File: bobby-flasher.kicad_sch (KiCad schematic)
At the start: 20 parts, among them J1 Conn_01x03, J2 Conn_01x06, J3 Flash, Q1 SS8050_C2150, Q2 SS8050_C2150, U1 CH343G, U2 AMS1117-3.3

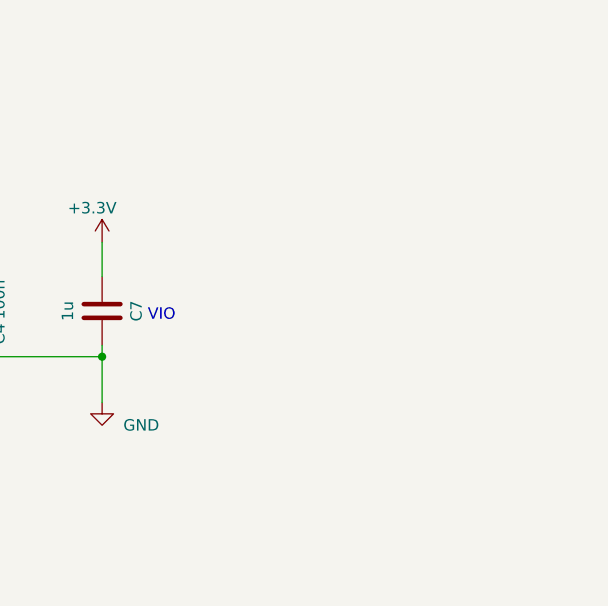
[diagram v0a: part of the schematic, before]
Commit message: new layout, added leds
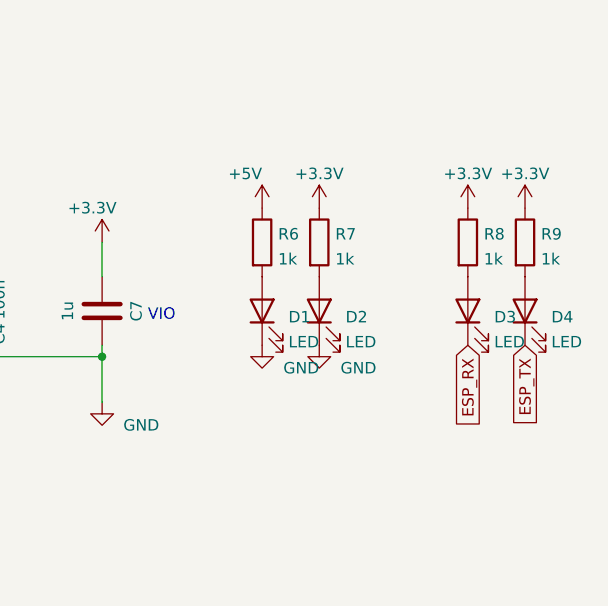
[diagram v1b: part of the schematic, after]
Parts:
- added D1, D2, D3, D4: LED, LED_SMD:LED_0603_1608Metric, symbol Device:LED
- added R6, R7, R8, R9: 1k, Resistor_SMD:R_0402_1005Metric, symbol Device:R
- C1, C3, C4, C6: footprint Capacitor_SMD:C_0603_1608Metric -> Capacitor_SMD:C_0402_1005Metric
- R1, R2, R3, R4, R5: footprint Resistor_SMD:R_0603_1608Metric -> Resistor_SMD:R_0402_1005Metric
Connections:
- net +3V3: now also R7.1, R8.1, R9.1
- net +5V: now also R6.1
- net ESP_RX: now also D3.1 (K)
- net ESP_TX: now also D4.1 (K)
- net GND: now also D1.1 (K), D2.1 (K)
- new net: D1.2 (A), R6.2
- new net: D3.2 (A), R8.2
- new net: D2.2 (A), R7.2
- new net: D4.2 (A), R9.2

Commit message: Updated files
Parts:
- C1, C3, C4, C6: LCSC Part # C14663 -> C1525
- D1: LCSC (none) -> C2286
- D2: LCSC (none) -> C72043
- D3: LCSC (none) -> C2290
- D4: LCSC (none) -> C72041
- J3: LCSC (none) -> C5663
- R1, R3: LCSC C23186 -> C25905
- R2: LCSC C25804 -> C25744
- R4, R5: LCSC C22790 -> C25752
- R6, R7, R8, R9: LCSC (none) -> C11702
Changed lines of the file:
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@@
       (effects (font (size 1.27 1.27)) hide)
     )
-    (property "LCSC Part #" "C14663" (id 4) (at 132.08 125.73 90)
+    (property "LCSC Part #" "C1525" (id 4) (at 132.08 125.73 90)
       (effects (font (size 1.27 1.27)) hide)
     )
@@
       (effects (font (size 1.27 1.27)) hide)
     )
-    (property "LCSC" "C22790" (id 4) (at 162.56 151.13 90)
+    (property "LCSC" "C25752" (id 4) (at 162.56 151.13 90)
       (effects (font (size 1.27 1.27)) hide)
     )
@@
     )
     (property "Datasheet" "~" (id 3) (at 166.37 88.9 0)
+      (effects (font (size 1.27 1.27)) hide)
+    )
+    (property "LCSC" "C11702" (id 4) (at 166.37 88.9 0)
       (effects (font (size 1.27 1.27)) hide)
     )
@@
       (effects (font (size 1.27 1.27)) hide)
     )
-    (property "LCSC Part #" "C14663" (id 4) (at 93.98 180.34 90)
+    (property "LCSC Part #" "C1525" (id 4) (at 93.98 180.34 90)
       (effects (font (size 1.27 1.27)) hide)
     )
@@
     )
     (property "Datasheet" "~" (id 3) (at 189.23 96.52 0)
+      (effects (font (size 1.27 1.27)) hide)
+    )
+    (property "LCSC" "C2290" (id 4) (at 189.23 96.52 90)
       (effects (font (size 1.27 1.27)) hide)
     )
@@
       (effects (font (size 1.27 1.27)) hide)
     )
+    (property "LCSC" "C2286" (id 4) (at 166.37 96.52 90)
+      (effects (font (size 1.27 1.27)) hide)
+    )
     (pin "1")
     (pin "2")
@@
       (effects (font (size 1.27 1.27)) hide)
     )
+    (property "LCSC" "C72043" (id 4) (at 172.72 96.52 90)
+      (effects (font (size 1.27 1.27)) hide)
+    )
     (pin "1")
     (pin "2")
@@
     )
     (property "Datasheet" "~" (id 3) (at 195.58 88.9 0)
+      (effects (font (size 1.27 1.27)) hide)
+    )
+    (property "LCSC" "C11702" (id 4) (at 195.58 88.9 0)
       (effects (font (size 1.27 1.27)) hide)
     )
@@
       (effects (font (size 1.27 1.27)) hide)
     )
+    (property "LCSC" "C72041" (id 4) (at 195.58 96.52 90)
+      (effects (font (size 1.27 1.27)) hide)
+    )
     (pin "1")
     (pin "2")
@@
       (effects (font (size 1.27 1.27)) hide)
     )
+    (property "LCSC" "C11702" (id 4) (at 189.23 88.9 0)
+      (effects (font (size 1.27 1.27)) hide)
+    )
     (pin "1")
     (pin "2")
@@
       (effects (font (size 1.27 1.27)) hide)
     )
-    (property "LCSC" "C23186" (id 4) (at 66.04 167.64 90)
+    (property "LCSC" "C25905" (id 4) (at 66.04 167.64 90)
       (effects (font (size 1.27 1.27)) hide)
     )
@@
       (effects (font (size 1.27 1.27)) hide)
     )
-    (property "LCSC" "C23186" (id 4) (at 33.02 167.64 90)
+    (property "LCSC" "C25905" (id 4) (at 33.02 167.64 90)
       (effects (font (size 1.27 1.27)) hide)
     )
@@
       (effects (font (size 1.27 1.27)) hide)
     )
-    (property "LCSC" "C22790" (id 4) (at 162.56 137.16 90)
+    (property "LCSC" "C25752" (id 4) (at 162.56 137.16 90)
       (effects (font (size 1.27 1.27)) hide)
     )
@@
       (effects (font (size 1.27 1.27)) hide)
     )
-    (property "LCSC Part #" "C14663" (id 4) (at 147.32 180.34 90)
+    (property "LCSC Part #" "C1525" (id 4) (at 147.32 180.34 90)
       (effects (font (size 1.27 1.27)) hide)
     )
@@
       (effects (font (size 1.27 1.27)) hide)
     )
-    (property "LCSC" "C25804" (id 4) (at 48.26 90.17 90)
+    (property "LCSC" "C25744" (id 4) (at 48.26 90.17 90)
       (effects (font (size 1.27 1.27)) hide)
     )
@@
       (effects (font (size 1.27 1.27)) hide)
     )
+    (property "LCSC" "C5663" (id 4) (at 107.95 87.63 0)
+      (effects (font (size 1.27 1.27)) hide)
+    )
     (pin "1")
     (pin "2")
@@
       (effects (font (size 1.27 1.27)) hide)
     )
-    (property "LCSC Part #" "C14663" (id 4) (at 133.35 96.52 90)
+    (property "LCSC Part #" "C1525" (id 4) (at 133.35 96.52 90)
       (effects (font (size 1.27 1.27)) hide)
     )
@@
       (effects (font (size 1.27 1.27)) hide)
     )
+    (property "LCSC" "C11702" (id 4) (at 172.72 88.9 0)
+      (effects (font (size 1.27 1.27)) hide)
+    )

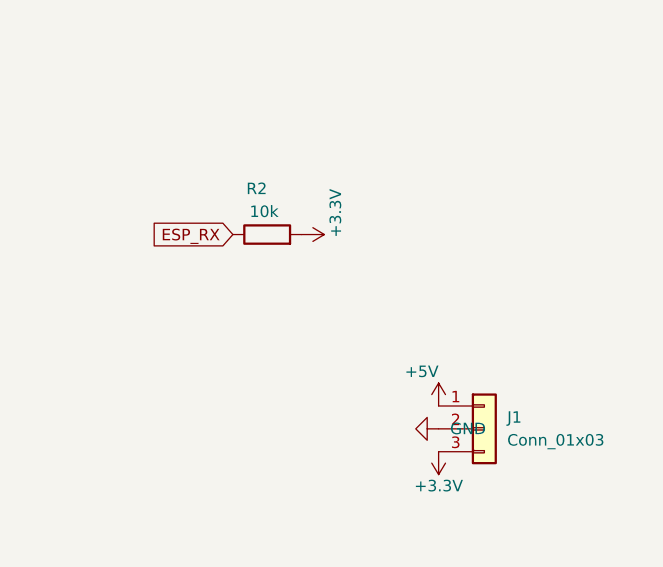
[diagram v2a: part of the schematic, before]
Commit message: Added 10k pullup to DTR
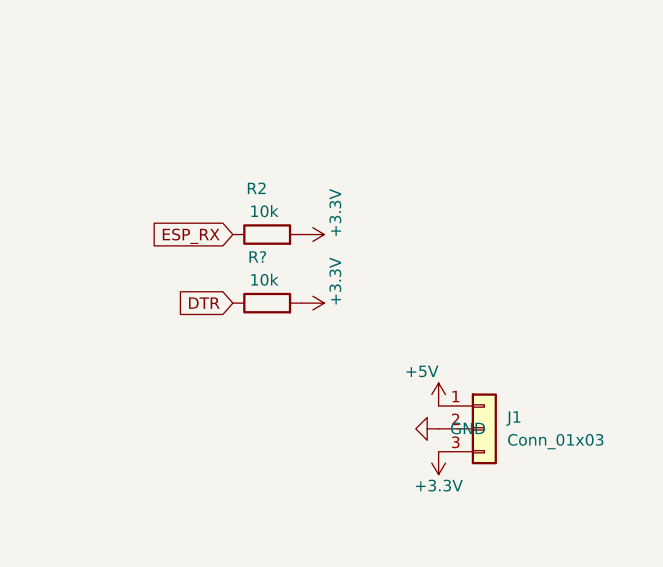
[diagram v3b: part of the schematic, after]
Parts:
- added R?: 10k, Resistor_SMD:R_0402_1005Metric, symbol Device:R
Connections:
- net +3V3: now also R?.2
- net DTR: now also R?.1
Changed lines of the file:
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@@
+    )
+  )
+  (global_label "DTR" (shape input) (at 44.45 97.79 180) (fields_autoplaced)
+    (effects (font (size 1.27 1.27)) (justify right))
+    (property "Referenzen zwischen Schaltplänen" "${INTERSHEET_REFS}" (id 0) (at 38.5293 97.7106 0)
+      (effects (font (size 1.27 1.27)) (justify right) hide)
     )
   )
@@
     (pin "2")
   )
+  (symbol (lib_id "power:+3.3V") (at 52.07 97.79 270) (unit 1)
+    (in_bom yes) (on_board yes)
+    (property "Reference" "#PWR?" (id 0) (at 48.26 97.79 0)
+      (effects (font (size 1.27 1.27)) hide)
+    )
+    (property "Value" "+3.3V" (id 1) (at 55.88 92.71 0)
+      (effects (font (size 1.27 1.27)) (justify left))
+    )
+    (property "Footprint" "" (id 2) (at 52.07 97.79 0)
+      (effects (font (size 1.27 1.27)) hide)
+    )
+    (property "Datasheet" "" (id 3) (at 52.07 97.79 0)
+      (effects (font (size 1.27 1.27)) hide)
+    )
+    (pin "1")
+  )
   (symbol (lib_id "power:GND") (at 102.87 60.96 270) (unit 1)
     (in_bom yes) (on_board yes)
@@
     )
     (pin "1")
+  )
+  (symbol (lib_id "Device:R") (at 48.26 97.79 90) (unit 1)
+    (in_bom yes) (on_board yes)
+    (property "Reference" "R?" (id 0) (at 48.26 92.71 90)
+      (effects (font (size 1.27 1.27)) (justify left))
+    )
+    (property "Value" "10k" (id 1) (at 49.53 95.25 90)
+      (effects (font (size 1.27 1.27)) (justify left))
+    )
+    (property "Footprint" "Resistor_SMD:R_0402_1005Metric" (id 2) (at 48.26 99.568 90)
+      (effects (font (size 1.27 1.27)) hide)
+    )
+    (property "Datasheet" "~" (id 3) (at 48.26 97.79 0)
+      (effects (font (size 1.27 1.27)) hide)
+    )
+    (property "LCSC" "C25744" (id 4) (at 48.26 97.79 90)
+      (effects (font (size 1.27 1.27)) hide)
+    )
+    (pin "1")
+    (pin "2")
   )
   (symbol (lib_id "power:GND") (at 29.21 167.64 270) (unit 1)
@@
       (reference "#PWR0133") (unit 1) (value "+3.3V") (footprint "")
     )
+    (path "/74147b9c-cb2f-4891-9443-1a94de746fa2"
+      (reference "#PWR?") (unit 1) (value "+3.3V") (footprint "")
+    )
     (path "/34194ef4-e853-4693-8338-89bc6f8fe21a"
       (reference "C1") (unit 1) (value "100n") (footprint "Capacitor_SMD:C_0402_1005Metric")
@@
       (reference "R9") (unit 1) (value "1k") (footprint "Resistor_SMD:R_0402_1005Metric")
     )
+    (path "/8d8a5fb8-3d37-44db-8066-f39f047239fe"
+      (reference "R?") (unit 1) (value "10k") (footprint "Resistor_SMD:R_0402_1005Metric")
+    )
     (path "/ae033daf-360c-4132-9495-c228de33337f"

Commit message: Updated schematic
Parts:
- gave numbers to parts that had none: 1
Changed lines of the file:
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@@
   (symbol (lib_id "power:+3.3V") (at 52.07 97.79 270) (unit 1)
     (in_bom yes) (on_board yes)
-    (property "Reference" "#PWR?" (id 0) (at 48.26 97.79 0)
+    (property "Reference" "#PWR0134" (id 0) (at 48.26 97.79 0)
       (effects (font (size 1.27 1.27)) hide)
     )
@@
   (symbol (lib_id "Device:R") (at 48.26 97.79 90) (unit 1)
     (in_bom yes) (on_board yes)
-    (property "Reference" "R?" (id 0) (at 48.26 92.71 90)
+    (property "Reference" "R10" (id 0) (at 48.26 92.71 90)
       (effects (font (size 1.27 1.27)) (justify left))
     )
@@
     )
     (path "/74147b9c-cb2f-4891-9443-1a94de746fa2"
-      (reference "#PWR?") (unit 1) (value "+3.3V") (footprint "")
+      (reference "#PWR0134") (unit 1) (value "+3.3V") (footprint "")
     )
     (path "/34194ef4-e853-4693-8338-89bc6f8fe21a"
@@
     )
     (path "/8d8a5fb8-3d37-44db-8066-f39f047239fe"
-      (reference "R?") (unit 1) (value "10k") (footprint "Resistor_SMD:R_0402_1005Metric")
+      (reference "R10") (unit 1) (value "10k") (footprint "Resistor_SMD:R_0402_1005Metric")
     )
     (path "/ae033daf-360c-4132-9495-c228de33337f"
